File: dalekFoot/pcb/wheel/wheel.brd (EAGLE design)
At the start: 100.3 x 100 mm, 75 parts, among them IC1 LM1117MP-3.3, IC3 LM1117MP-3.3, IC4 4051D, IC5 4051D, IC6 LM1117MP-3.3, U1 TB6612FNG(O,C,8,EL, U2 SS8050-SOT-23, U3 SS8050-SOT-23, U4 SS8050-SOT-23, U5 TB6612FNG(O,C,8,EL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

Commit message: update jlc chck file and bugfix
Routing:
- net BAT+: track 116.8 -> 117.7 mm
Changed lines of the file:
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@@
 <?xml version="1.0" encoding="utf-8"?>
 <!DOCTYPE eagle SYSTEM "eagle.dtd">
-<eagle version="8.2.1">
+<eagle version="7.2.0">
 <drawing>
 <settings>
@@
 <setting verticaltext="up"/>
 </settings>
-<grid distance="50" unitdist="mil" unit="mm" style="lines" multiple="1" display="yes" altdistance="0.025" altunitdist="inch" altunit="inch"/>
+<grid distance="5" unitdist="mil" unit="mil" style="lines" multiple="1" display="yes" altdistance="0.025" altunitdist="inch" altunit="inch"/>
 <layers>
 <layer number="1" name="Top" color="4" fill="1" visible="yes" active="yes"/>
@@
 </class>
 </classes>
-<designrules name="default">
-<description language="de">&lt;b&gt;EAGLE Design Rules&lt;/b&gt;
+<designrules name="szjlc-2021">
+<description language="en">&lt;b&gt;EAGLE Design Rules&lt;/b&gt;
 &lt;p&gt;
 Die Standard-Design-Rules sind so gewählt, dass sie für
@@
 besondere Anforderungen haben, treffen Sie die erforderlichen
 Einstellungen hier und speichern die Design Rules unter
-einem neuen Namen ab.</description>
-<description language="en">&lt;b&gt;EAGLE Design Rules&lt;/b&gt;
+einem neuen Namen ab.&lt;br /&gt;
+&lt;a href=&quot;https://www.jlc.com/portal/vtechnology.html&quot;&gt;https://www.jlc.com/portal/vtechnology.html&lt;/a&gt;</description>
+<description language="zh">&lt;b&gt;EAGLE Design Rules&lt;/b&gt;
 &lt;p&gt;
-The default Design Rules have been set to cover
-a wide range of applications. Your particular design
-may have different requirements, so please make the
-necessary adjustments and save your customized
-design rules under a new name.</description>
+Die Standard-Design-Rules sind so gewählt, dass sie für
+die meisten Anwendungen passen. Sollte ihre Platine
+besondere Anforderungen haben, treffen Sie die erforderlichen
+Einstellungen hier und speichern die Design Rules unter
+einem neuen Namen ab.&lt;br /&gt;
+&lt;a href=&quot;https://www.jlc.com/portal/vtechnology.html&quot;&gt;https://www.jlc.com/portal/vtechnology.html&lt;/a&gt;</description>
 <param name="layerSetup" value="(1*16)"/>
 <param name="mtCopper" value="0.035mm 0.035mm 0.035mm 0.035mm 0.035mm 0.035mm 0.035mm 0.035mm 0.035mm 0.035mm 0.035mm 0.035mm 0.035mm 0.035mm 0.035mm 0.035mm"/>
 <param name="mtIsolate" value="1.5mm 0.15mm 0.2mm 0.15mm 0.2mm 0.15mm 0.2mm 0.15mm 0.2mm 0.15mm 0.2mm 0.15mm 0.2mm 0.15mm 0.2mm"/>
 <param name="mdWireWire" value="5mil"/>
-<param name="mdWirePad" value="6mil"/>
-<param name="mdWireVia" value="6mil"/>
-<param name="mdPadPad" value="6mil"/>
-<param name="mdPadVia" value="6mil"/>
-<param name="mdViaVia" value="6mil"/>
-<param name="mdSmdPad" value="6mil"/>
-<param name="mdSmdVia" value="6mil"/>
-<param name="mdSmdSmd" value="6mil"/>
-<param name="mdViaViaSameLayer" value="6mil"/>
+<param name="mdWirePad" value="5mil"/>
+<param name="mdWireVia" value="5mil"/>
+<param name="mdPadPad" value="5mil"/>
+<param name="mdPadVia" value="5mil"/>
+<param name="mdViaVia" value="5mil"/>
+<param name="mdSmdPad" value="5mil"/>
+<param name="mdSmdVia" value="5mil"/>
+<param name="mdSmdSmd" value="5mil"/>
+<param name="mdViaViaSameLayer" value="8mil"/>
 <param name="mnLayersViaInSmd" value="2"/>
-<param name="mdCopperDimension" value="40mil"/>
-<param name="mdDrill" value="6mil"/>
+<param name="mdCopperDimension" value="0.2mm"/>
+<param name="mdDrill" value="8mil"/>
 <param name="mdSmdStop" value="0mil"/>
 <param name="msWidth" value="5mil"/>
-<param name="msDrill" value="0.35mm"/>
+<param name="msDrill" value="0.2mm"/>
 <param name="msMicroVia" value="9.99mm"/>
 <param name="msBlindViaRatio" value="0.5"/>
@@
 <param name="rvMicroViaOuter" value="0.25"/>
 <param name="rvMicroViaInner" value="0.25"/>
-<param name="rlMinPadTop" value="10mil"/>
+<param name="rlMinPadTop" value="3mil"/>
 <param name="rlMaxPadTop" value="20mil"/>
-<param name="rlMinPadInner" value="10mil"/>
+<param name="rlMinPadInner" value="3mil"/>
 <param name="rlMaxPadInner" value="20mil"/>
-<param name="rlMinPadBottom" value="10mil"/>
+<param name="rlMinPadBottom" value="3mil"/>
 <param name="rlMaxPadBottom" value="20mil"/>
-<param name="rlMinViaOuter" value="8mil"/>
+<param name="rlMinViaOuter" value="3mil"/>
 <param name="rlMaxViaOuter" value="20mil"/>
-<param name="rlMinViaInner" value="8mil"/>
+<param name="rlMinViaInner" value="3mil"/>
 <param name="rlMaxViaInner" value="20mil"/>
-<param name="rlMinMicroViaOuter" value="4mil"/>
+<param name="rlMinMicroViaOuter" value="3mil"/>
 <param name="rlMaxMicroViaOuter" value="20mil"/>
-<param name="rlMinMicroViaInner" value="4mil"/>
+<param name="rlMinMicroViaInner" value="3mil"/>
 <param name="rlMaxMicroViaInner" value="20mil"/>
 <param name="psTop" value="-1"/>
@@
 <param name="mvStopFrame" value="1"/>
 <param name="mvCreamFrame" value="0"/>
-<param name="mlMinStopFrame" value="4mil"/>
+<param name="mlMinStopFrame" value="2mil"/>
 <param name="mlMaxStopFrame" value="4mil"/>
 <param name="mlMinCreamFrame" value="0mil"/>
 <param name="mlMaxCreamFrame" value="0mil"/>
-<param name="mlViaStopLimit" value="0mil"/>
+<param name="mlViaStopLimit" value="0.7mm"/>
 <param name="srRoundness" value="0"/>
 <param name="srMinRoundness" value="0mil"/>
@@
 <wire x1="40.64" y1="34.29" x2="46.99" y2="34.29" width="1.016" layer="1"/>
 <wire x1="40.875" y1="34.525" x2="40.64" y2="34.29" width="1.016" layer="1"/>
-<wire x1="40.64" y1="37.68" x2="40.64" y2="34.29" width="1.016" layer="1"/>
-<wire x1="40.64" y1="37.68" x2="40.6646" y2="37.7046" width="1.016" layer="1"/>
-<wire x1="40.875" y1="37.915" x2="40.6646" y2="37.7046" width="1.016" layer="1" curve="0.9" cap="flat"/>
+<wire x1="40.64" y1="38.442" x2="40.64" y2="37.973" width="1.016" layer="1"/>
+<wire x1="40.64" y1="37.973" x2="40.64" y2="34.29" width="1.016" layer="1"/>
 <wire x1="46.99" y1="34.29" x2="48.025" y2="35.325" width="1.016" layer="1"/>
 <wire x1="48.025" y1="37.915" x2="48.025" y2="35.325" width="1.016" layer="1"/>
@@
 <wire x1="53.34" y1="34.29" x2="60.96" y2="34.29" width="1.016" layer="1"/>
 <wire x1="60.96" y1="37.68" x2="60.96" y2="34.29" width="1.016" layer="1"/>
-<wire x1="53.34" y1="37.68" x2="53.34" y2="34.29" width="1.016" layer="1"/>
-<wire x1="53.34" y1="37.68" x2="53.3646" y2="37.7046" width="1.016" layer="1"/>
-<wire x1="53.575" y1="37.915" x2="53.34" y2="37.68" width="1.016" layer="1" curve="0.5" cap="flat"/>
+<wire x1="53.34" y1="38.188" x2="53.34" y2="37.973" width="1.016" layer="1"/>
+<wire x1="53.34" y1="37.973" x2="53.34" y2="34.29" width="1.016" layer="1"/>
 <wire x1="60.075" y1="37.915" x2="60.725" y2="37.915" width="1.016" layer="1" curve="0.5" cap="flat"/>
 <wire x1="60.725" y1="37.915" x2="60.96" y2="37.68" width="1.016" layer="1"/>
@@
 <wire x1="67.31" y1="37.68" x2="67.31" y2="34.29" width="1.016" layer="1"/>
 <wire x1="67.31" y1="37.68" x2="67.3346" y2="37.7046" width="1.016" layer="1"/>
-<wire x1="67.545" y1="37.915" x2="67.31" y2="37.68" width="1.016" layer="1" curve="0.5" cap="flat"/>
+<wire x1="40.875" y1="37.915" x2="40.64" y2="37.915" width="0.4064" layer="1"/>
+<wire x1="40.64" y1="37.915" x2="40.64" y2="37.973" width="0.4064" layer="1"/>
+<wire x1="53.575" y1="37.915" x2="53.34" y2="37.915" width="0.4064" layer="1"/>
+<wire x1="53.34" y1="37.915" x2="53.34" y2="37.973" width="0.4064" layer="1"/>
+<wire x1="67.3346" y1="37.7046" x2="67.545" y2="37.915" width="0" layer="19" extent="1-1"/>
 </signal>
 <signal name="VCC-DIGITAL">

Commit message: modify u1 bug and IRT
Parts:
- moved R35 1.45 mm to (92.3, 53.5), turned to 270 degrees
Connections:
- net PWM1.B: now also U1.15
- net PWM2.B: no longer U1.15
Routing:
- net VCC-IRT: track 93.5 -> 191.0 mm, vias 2 -> 0
- net USART_TX: track 126.8 -> 99.1 mm, vias 0 -> 1
- net PWM1.B: track 0.00 -> 26.5 mm, vias 0 -> 2
- net USART_RX: track 114.5 -> 95.0 mm, vias 0 -> 1
- net PWM2.B: track 31.5 -> 16.1 mm, vias 2 -> 0
- net DGND: track 781.5 -> 795.3 mm
- net AO1.2: track 23.7 -> 16.2 mm
- net N$6: track 21.7 -> 26.0 mm
- net BO3.1: track 16.0 -> 13.1 mm
- net BO3.2: track 21.9 -> 20.4 mm, vias 2 -> 1
- net AO1.1: track 21.3 -> 20.3 mm

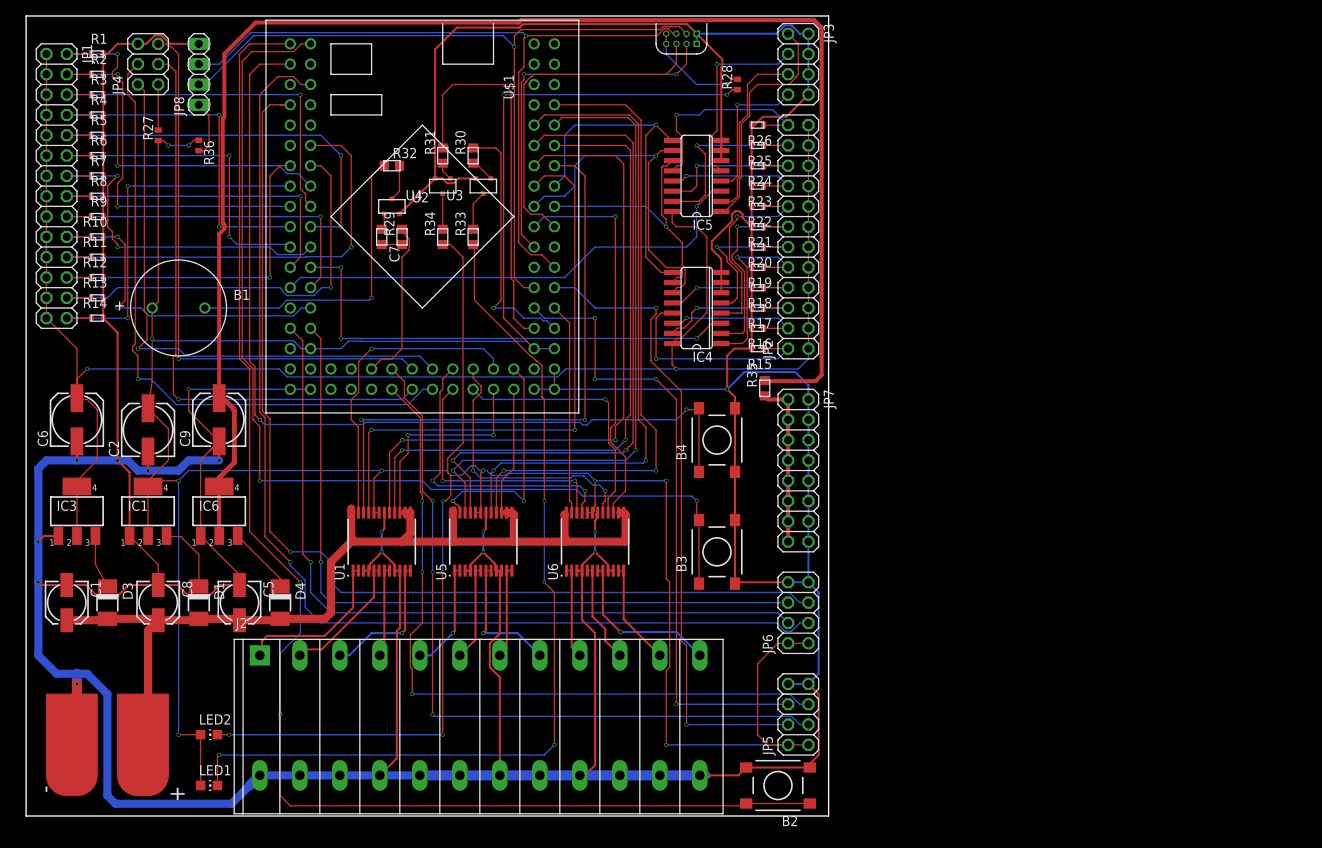
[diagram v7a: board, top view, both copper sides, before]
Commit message: resixe dimension to 100 x 100
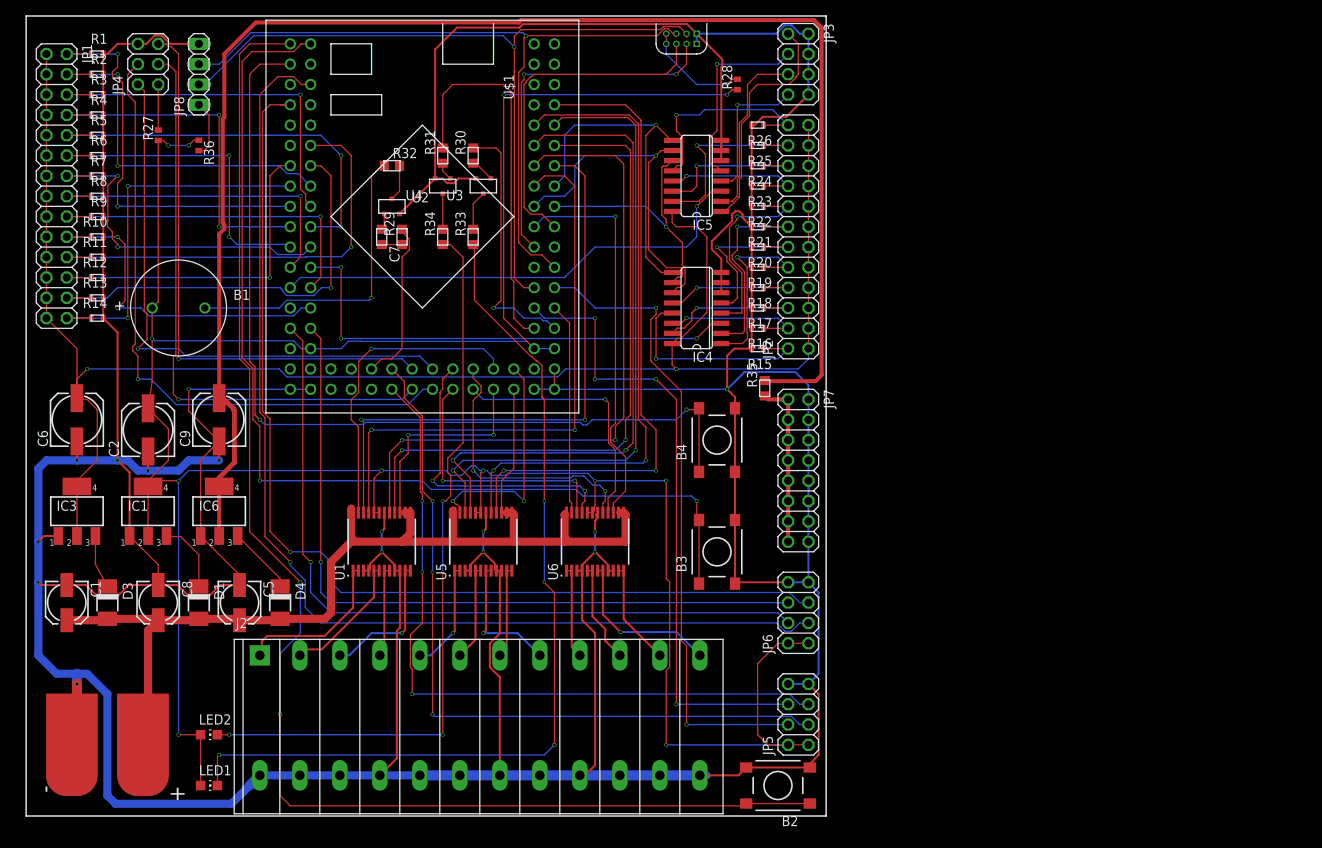
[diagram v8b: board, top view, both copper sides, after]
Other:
- board size 100.3 x 100 mm -> 100 x 100 mm
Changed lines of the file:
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@@
 <?xml version="1.0" encoding="utf-8"?>
 <!DOCTYPE eagle SYSTEM "eagle.dtd">
-<eagle version="8.2.1">
+<eagle version="7.2.0">
 <drawing>
 <settings>
@@
 <setting verticaltext="up"/>
 </settings>
-<grid distance="5" unitdist="mil" unit="mil" style="lines" multiple="1" display="yes" altdistance="0.025" altunitdist="inch" altunit="inch"/>
+<grid distance="5" unitdist="mil" unit="mm" style="lines" multiple="1" display="yes" altdistance="0.025" altunitdist="inch" altunit="inch"/>
 <layers>
 <layer number="1" name="Top" color="4" fill="1" visible="yes" active="yes"/>
@@
 <board>
 <plain>
-<wire x1="0" y1="0" x2="100.31" y2="0" width="0" layer="20"/>
-<wire x1="100.31" y1="0" x2="100.31" y2="100" width="0" layer="20"/>
-<wire x1="100.31" y1="100" x2="0" y2="100" width="0" layer="20"/>
+<wire x1="0" y1="0" x2="100" y2="0" width="0" layer="20"/>
+<wire x1="100" y1="0" x2="100" y2="100" width="0" layer="20"/>
+<wire x1="100" y1="100" x2="0" y2="100" width="0" layer="20"/>
 <wire x1="0" y1="100" x2="0" y2="0" width="0" layer="20"/>
 </plain>
